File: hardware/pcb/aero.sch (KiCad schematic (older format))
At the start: 2 parts

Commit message: more progress on hw
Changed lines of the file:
@@
 $Descr A4 11693 8268
 encoding utf-8
-Sheet 1 5
+Sheet 1 6
 Title ""
 Date ""
@@
 $EndSheet
 $Sheet
-S 1950 850  700  650
+S 1250 3750 700  650
 U 551EEA41
 F0 "ms5611" 60
 F1 "ms5611.sch" 60
-F2 "EN" I R 2650 1150 60
-F3 "SCLK" I R 2650 1450 60
-F4 "MOSI" I R 2650 1250 60
-F5 "MISO" I R 2650 1350 60
-$EndSheet
-$Sheet
-S 1850 2650 750  900
+F2 "EN" I R 1950 4050 60
+F3 "SCLK" I R 1950 4350 60
+F4 "MOSI" I R 1950 4150 60
+F5 "MISO" I R 1950 4250 60
+$EndSheet
+$Sheet
+S 1300 4800 750  900
 U 5527E8E0
 F0 "bmx055" 60
 F1 "bmx055.sch" 60
-F2 "ACC_SEL" I R 2600 2750 60
-F3 "GYRO_SEL" I R 2600 2850 60
-F4 "MAG_SEL" I R 2600 2950 60
-F5 "ACC_INT" I R 2600 3050 60
-F6 "MISO" I R 2600 3250 60
-F7 "MOSI" I R 2600 3350 60
-F8 "SCK" I R 2600 3450 60
+F2 "ACC_SEL" I R 2050 4900 60
+F3 "GYRO_SEL" I R 2050 5000 60
+F4 "MAG_SEL" I R 2050 5100 60
+F5 "ACC_INT" I R 2050 5200 60
+F6 "MISO" I R 2050 5400 60
+F7 "MOSI" I R 2050 5500 60
+F8 "SCK" I R 2050 5600 60
 $EndSheet
 $Comp
@@
 	9100 2600 9100 3900
 Connection ~ 9100 3900
+$Sheet
+S 1500 1450 800  650
+U 552EDA4D
+F0 "power" 60
+F1 "power.sch" 60
+F2 "+3V" I R 2300 1600 60
+F3 "USB_D-" I R 2300 1750 60
+F4 "USB_D+" I R 2300 1850 60
+$EndSheet
+$Comp
+L +3V #PWR?
+U 1 1 552F0919
+P 2800 1300
+F 0 "#PWR?" H 2800 1200 60  0001 C CNN
+F 1 "+3V" H 2650 1450 60  0000 C CNN
+F 2 "" H 2800 1300 60  0000 C CNN
+F 3 "" H 2800 1300 60  0000 C CNN
+	1    2800 1300
+	1    0    0    -1
+$EndComp
+Wire Wire Line
+	2800 1300 2800 1600
+Wire Wire Line
+	2800 1600 2300 1600
 $EndSCHEMATC

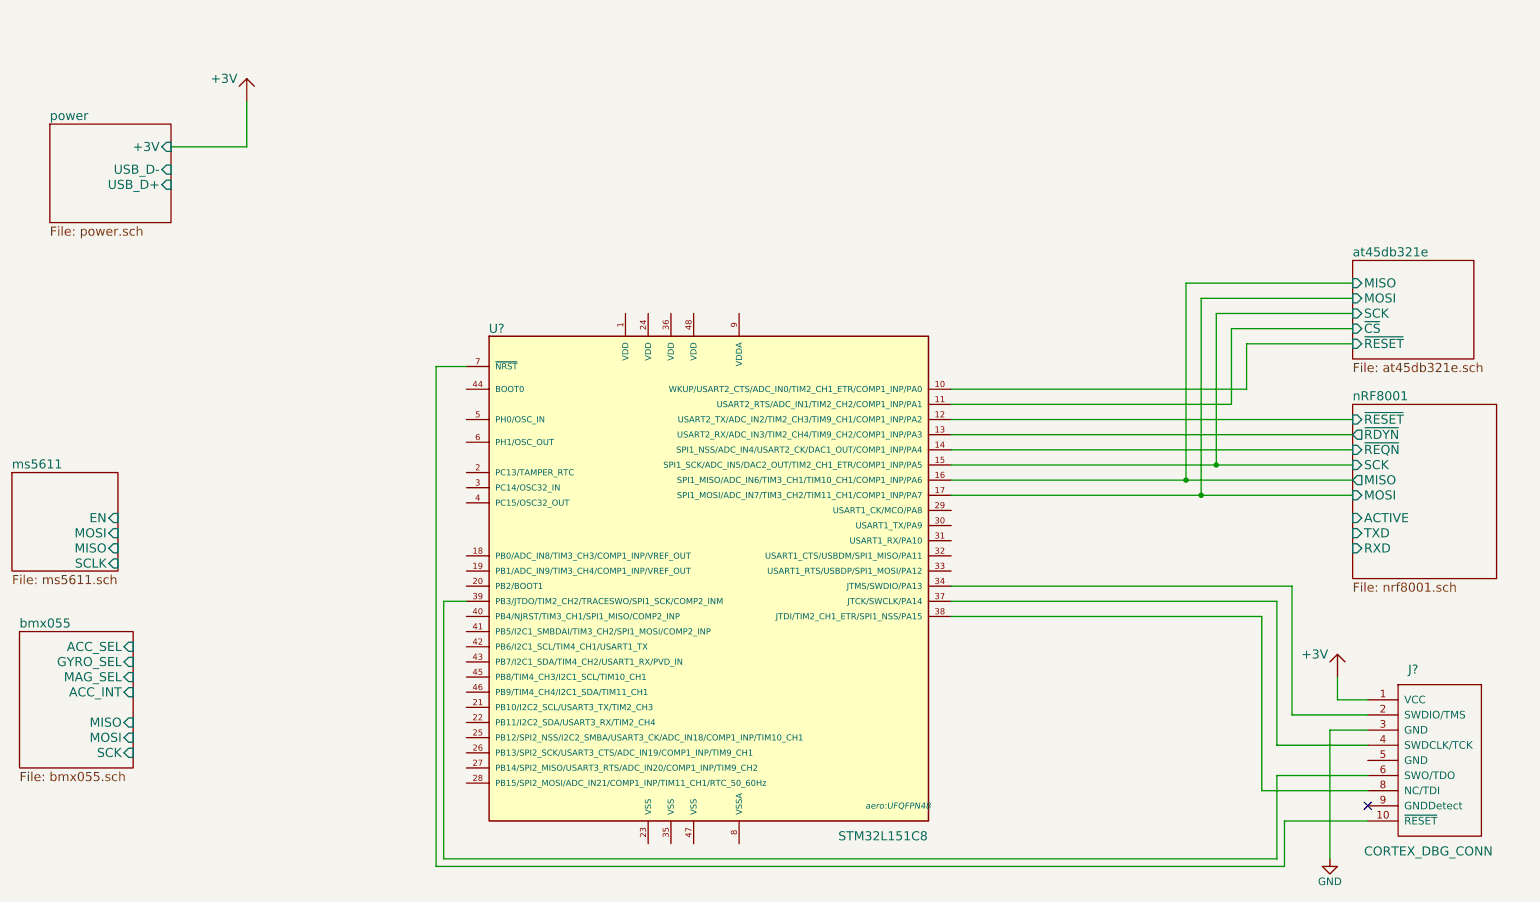
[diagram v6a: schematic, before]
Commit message: More work on power section
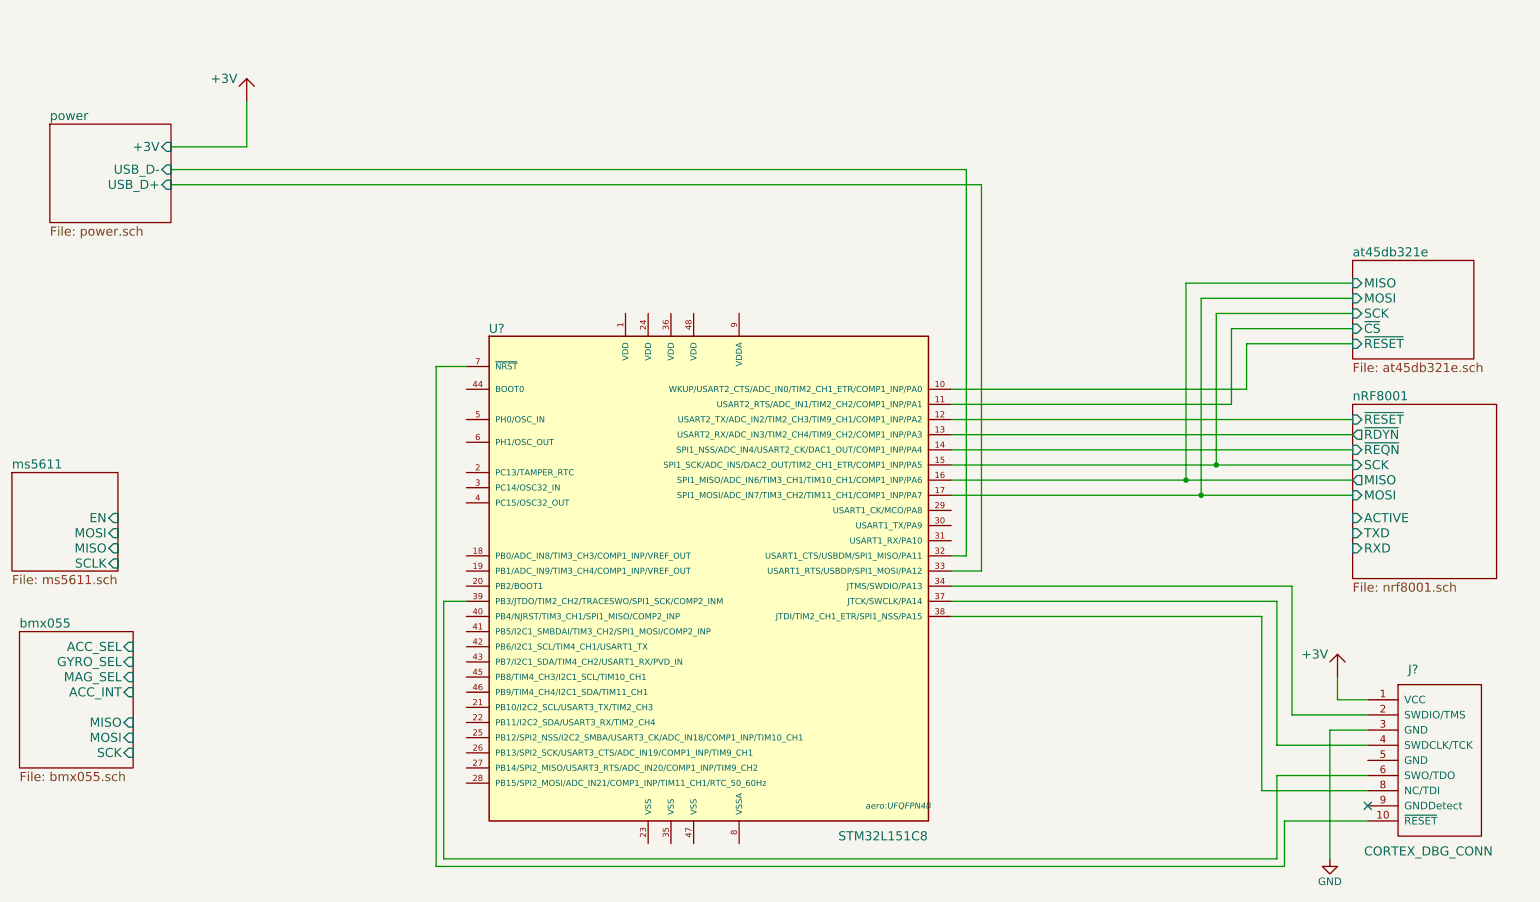
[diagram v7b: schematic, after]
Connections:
- net power/USB_D+: now also U?.33 (USART1_RTS/USBDP/SPI1_MOSI/PA12)
- net power/USB_D-: now also U?.32 (USART1_CTS/USBDM/SPI1_MISO/PA11)
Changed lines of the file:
@@
 Wire Wire Line
 	2800 1600 2300 1600
+Wire Wire Line
+	2300 1750 7550 1750
+Wire Wire Line
+	7550 1750 7550 4300
+Wire Wire Line
+	7550 4300 7450 4300
+Wire Wire Line
+	7450 4400 7650 4400
+Wire Wire Line
+	7650 4400 7650 1850
+Wire Wire Line
+	7650 1850 2300 1850
 $EndSCHEMATC

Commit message: added sensor connections
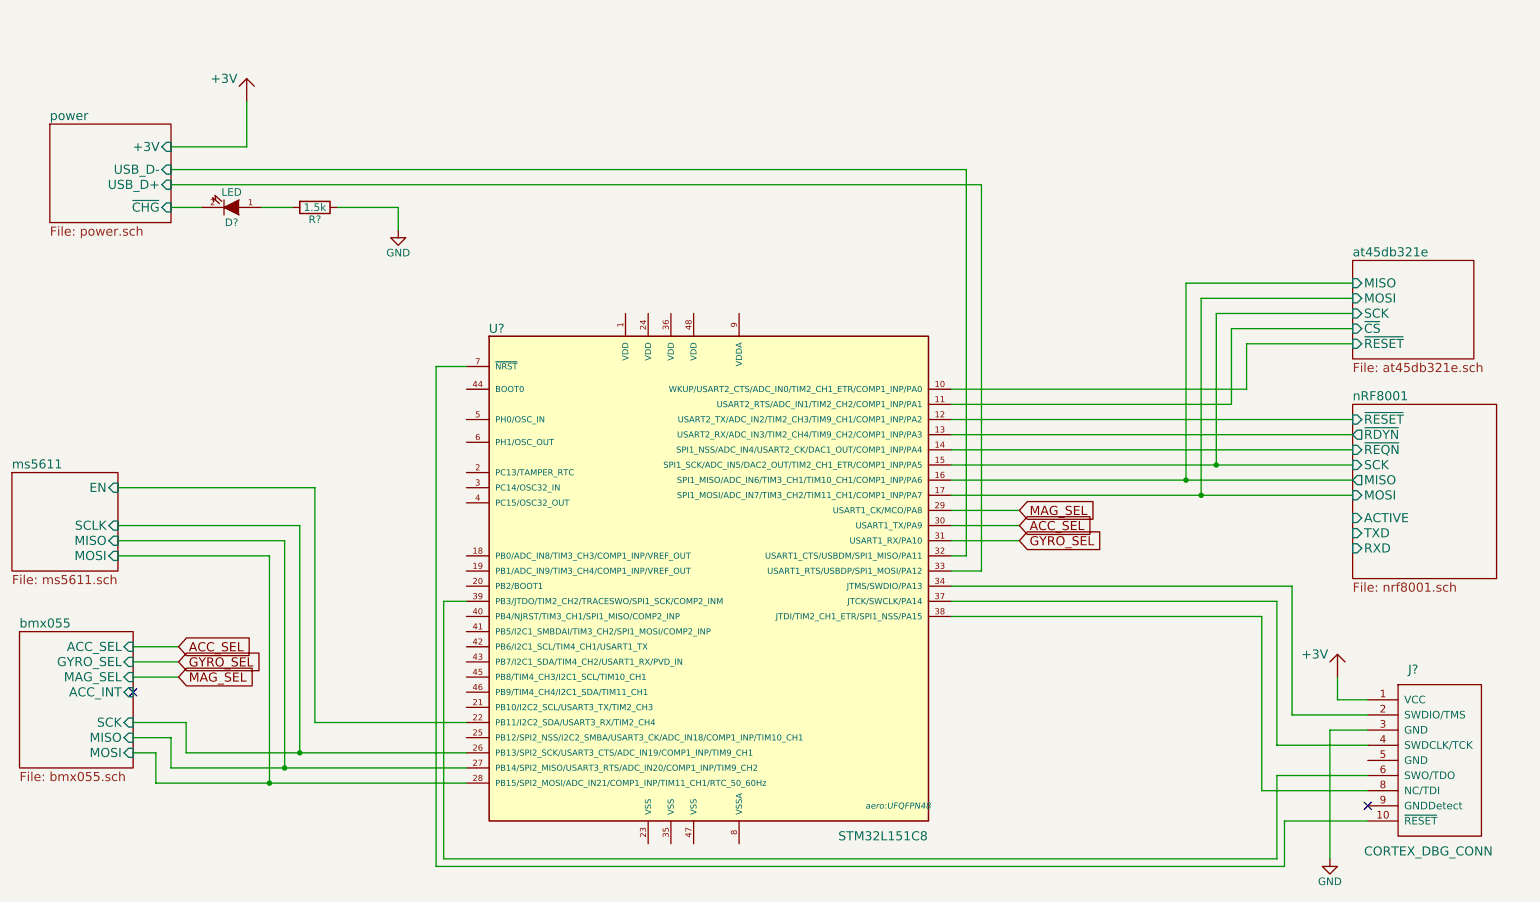
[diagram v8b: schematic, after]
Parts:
- added D?: LED, symbol LED
- added R?: 1.5k, symbol R
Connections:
- net GND: now also R?.1
- net bmx055/MISO: now also U?.27 (PB14/SPI2_MISO/USART3_RTS/ADC_IN20/COMP1_INP/TIM9_CH2)
- net bmx055/MOSI: now also U?.28 (PB15/SPI2_MOSI/ADC_IN21/COMP1_INP/TIM11_CH1/RTC_50_60Hz)
- net bmx055/SCK: now also U?.26 (PB13/SPI2_SCK/USART3_CTS/ADC_IN19/COMP1_INP/TIM9_CH1)
- net ms5611/EN: now also U?.22 (PB11/I2C2_SDA/USART3_RX/TIM2_CH4)
- net MAG_SEL: now reaches U?.29 (USART1_CK/MCO/PA8)
- net ACC_SEL: now reaches U?.30 (USART1_TX/PA9)
- net GYRO_SEL: now reaches U?.31 (USART1_RX/PA10)
- new net: D?.1 (A), R?.2
- new net power/~CHG: D?.2 (K)
- no-connect marks 1 -> 2
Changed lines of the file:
@@
 F0 "ms5611" 60
 F1 "ms5611.sch" 60
-F2 "EN" I R 1950 4050 60
-F3 "SCLK" I R 1950 4350 60
-F4 "MOSI" I R 1950 4150 60
-F5 "MISO" I R 1950 4250 60
+F2 "EN" I R 1950 3850 60
+F3 "SCLK" I R 1950 4100 60
+F4 "MOSI" I R 1950 4300 60
+F5 "MISO" I R 1950 4200 60
 $EndSheet
 $Sheet
@@
 F4 "MAG_SEL" I R 2050 5100 60
 F5 "ACC_INT" I R 2050 5200 60
-F6 "MISO" I R 2050 5400 60
-F7 "MOSI" I R 2050 5500 60
-F8 "SCK" I R 2050 5600 60
+F6 "MISO" I R 2050 5500 60
+F7 "MOSI" I R 2050 5600 60
+F8 "SCK" I R 2050 5400 60
 $EndSheet
 $Comp
@@
 F6 "~RESET" I L 10100 2900 60
 $EndSheet
-Wire Wire Line
-	10100 3900 7450 3900
-Wire Wire Line
-	7450 3700 10100 3700
-Wire Wire Line
-	10100 3800 7450 3800
-Wire Wire Line
-	7450 3600 10100 3600
-Wire Wire Line
-	10100 3500 7450 3500
-Wire Wire Line
-	7450 3400 10100 3400
-Wire Wire Line
-	10200 5250 10000 5250
-Wire Wire Line
-	10000 5250 10000 5100
-Wire Wire Line
-	10200 5350 9700 5350
-Wire Wire Line
-	9700 5350 9700 4500
-Wire Wire Line
-	9700 4500 7450 4500
-Wire Wire Line
-	7450 4600 9600 4600
-Wire Wire Line
-	9600 4600 9600 5550
-Wire Wire Line
-	9600 5550 10200 5550
-Wire Wire Line
-	4250 4600 4100 4600
-Wire Wire Line
-	4100 4600 4100 6300
-Wire Wire Line
-	4100 6300 9600 6300
-Wire Wire Line
-	9600 6300 9600 5750
-Wire Wire Line
-	9600 5750 10200 5750
-Wire Wire Line
-	7450 4700 9500 4700
-Wire Wire Line
-	9500 4700 9500 5850
-Wire Wire Line
-	9500 5850 10200 5850
-Wire Wire Line
-	10200 5450 9950 5450
-Wire Wire Line
-	9950 5450 9950 6300
-Wire Wire Line
-	10100 2500 9000 2500
-Wire Wire Line
-	9000 2500 9000 3800
-Connection ~ 9000 3800
-Wire Wire Line
-	10100 2700 9200 2700
-Wire Wire Line
-	9200 2700 9200 3700
-Connection ~ 9200 3700
-Wire Wire Line
-	10100 2800 9300 2800
-Wire Wire Line
-	9300 2800 9300 3300
-Wire Wire Line
-	9300 3300 7450 3300
-Wire Wire Line
-	10100 2900 9400 2900
-Wire Wire Line
-	9400 2900 9400 3200
-Wire Wire Line
-	9400 3200 7450 3200
-Wire Wire Line
-	10200 6050 9650 6050
-Wire Wire Line
-	9650 6050 9650 6350
-Wire Wire Line
-	9650 6350 4050 6350
-Wire Wire Line
-	4050 6350 4050 3050
-Wire Wire Line
-	4050 3050 4250 3050
-Wire Wire Line
-	10100 2600 9100 2600
-Wire Wire Line
-	9100 2600 9100 3900
-Connection ~ 9100 3900
 $Sheet
 S 1500 1450 800  650
@@
 F3 "USB_D-" I R 2300 1750 60
 F4 "USB_D+" I R 2300 1850 60
+F5 "~CHG" I R 2300 2000 60
 $EndSheet
 $Comp
@@
 	1    0    0    -1
 $EndComp
+$Comp
+L LED D?
+U 1 1 553048D5
+P 2700 2000
+F 0 "D?" H 2700 2100 50  0000 C CNN
+F 1 "LED" H 2700 1900 50  0000 C CNN
+F 2 "" H 2700 2000 60  0000 C CNN
+F 3 "" H 2700 2000 60  0000 C CNN
+	1    2700 2000
+	-1   0    0    1
+$EndComp
+$Comp
+L R R?
+U 1 1 553049A8
+P 3250 2000
+F 0 "R?" V 3330 2000 50  0000 C CNN
+F 1 "1.5k" V 3250 2000 50  0000 C CNN
+F 2 "" V 3180 2000 30  0000 C CNN
+F 3 "" H 3250 2000 30  0000 C CNN
+	1    3250 2000
+	0    1    1    0
+$EndComp
+$Comp
+L GND #PWR?
+U 1 1 55304B43
+P 3800 2150
+F 0 "#PWR?" H 3800 1900 50  0001 C CNN
+F 1 "GND" H 3800 2000 50  0000 C CNN
+F 2 "" H 3800 2150 60  0000 C CNN
+F 3 "" H 3800 2150 60  0000 C CNN
+	1    3800 2150
+	1    0    0    -1
+$EndComp
+Text GLabel 7900 4100 2    60   Input ~ 0
+ACC_SEL
+Text GLabel 7900 4200 2    60   Input ~ 0
+GYRO_SEL
+Text GLabel 7900 4000 2    60   Input ~ 0
+MAG_SEL
+Text GLabel 2350 5100 2    60   Input ~ 0
+MAG_SEL
+Text GLabel 2350 5000 2    60   Input ~ 0
+GYRO_SEL
+Text GLabel 2350 4900 2    60   Input ~ 0
+ACC_SEL
+Wire Wire Line
+	10100 3900 7450 3900
+Wire Wire Line
+	7450 3700 10100 3700
+Wire Wire Line
+	10100 3800 7450 3800
+Wire Wire Line
+	7450 3600 10100 3600
+Wire Wire Line
+	10100 3500 7450 3500
+Wire Wire Line
+	7450 3400 10100 3400
+Wire Wire Line
+	10200 5250 10000 5250
+Wire Wire Line
+	10000 5250 10000 5100
+Wire Wire Line
+	10200 5350 9700 5350
+Wire Wire Line
+	9700 5350 9700 4500
+Wire Wire Line
+	9700 4500 7450 4500
+Wire Wire Line
+	7450 4600 9600 4600
+Wire Wire Line
+	9600 4600 9600 5550
+Wire Wire Line
+	9600 5550 10200 5550
+Wire Wire Line
+	4250 4600 4100 4600
+Wire Wire Line
+	4100 4600 4100 6300
+Wire Wire Line
+	4100 6300 9600 6300
+Wire Wire Line
+	9600 6300 9600 5750
+Wire Wire Line
+	9600 5750 10200 5750
+Wire Wire Line
+	7450 4700 9500 4700
+Wire Wire Line
+	9500 4700 9500 5850
+Wire Wire Line
+	9500 5850 10200 5850
+Wire Wire Line
+	10200 5450 9950 5450
+Wire Wire Line
+	9950 5450 9950 6300
+Wire Wire Line
+	10100 2500 9000 2500
+Wire Wire Line
+	9000 2500 9000 3800
+Connection ~ 9000 3800
+Wire Wire Line
+	10100 2700 9200 2700
+Wire Wire Line
+	9200 2700 9200 3700
+Connection ~ 9200 3700
+Wire Wire Line
+	10100 2800 9300 2800
+Wire Wire Line
+	9300 2800 9300 3300
+Wire Wire Line
+	9300 3300 7450 3300
+Wire Wire Line
+	10100 2900 9400 2900
+Wire Wire Line
+	9400 2900 9400 3200
+Wire Wire Line
+	9400 3200 7450 3200
+Wire Wire Line
+	10200 6050 9650 6050
+Wire Wire Line
+	9650 6050 9650 6350
+Wire Wire Line
+	9650 6350 4050 6350
+Wire Wire Line
+	4050 6350 4050 3050
+Wire Wire Line
+	4050 3050 4250 3050
+Wire Wire Line
+	10100 2600 9100 2600
+Wire Wire Line
+	9100 2600 9100 3900
+Connection ~ 9100 3900
 Wire Wire Line
 	2800 1300 2800 1600
@@
 Wire Wire Line
 	7650 1850 2300 1850
+Wire Wire Line
+	3400 2000 3800 2000
+Wire Wire Line
+	3800 2000 3800 2150
+Wire Wire Line
+	3100 2000 2900 2000
+Wire Wire Line
+	2500 2000 2300 2000
+Wire Wire Line
+	7900 4000 7450 4000
+Wire Wire Line
+	7900 4100 7450 4100
+Wire Wire Line
+	7900 4200 7450 4200
+Wire Wire Line
+	2050 4900 2350 4900
+Wire Wire Line
+	2350 5000 2050 5000
+Wire Wire Line
+	2050 5100 2350 5100
+NoConn ~ 2050 5200
+Wire Wire Line
+	4250 5800 2200 5800
+Wire Wire Line
+	2200 5800 2200 5600
+Wire Wire Line
+	2200 5600 2050 5600
+Wire Wire Line
+	2050 5500 2300 5500
+Wire Wire Line
+	2300 5500 2300 5700
+Wire Wire Line
+	2300 5700 4250 5700
+Wire Wire Line
+	2050 5400 2400 5400
+Wire Wire Line
+	2400 5400 2400 5600
+Wire Wire Line
+	2400 5600 4250 5600
+Wire Wire Line
+	1950 4300 2950 4300
+Wire Wire Line
+	2950 4300 2950 5800
+Connection ~ 2950 5800
+Wire Wire Line
+	1950 4200 3050 4200
+Wire Wire Line
+	3050 4200 3050 5700
+Connection ~ 3050 5700
+Wire Wire Line
+	1950 4100 3150 4100
+Wire Wire Line
+	3150 4100 3150 5600
+Connection ~ 3150 5600
+Wire Wire Line
+	1950 3850 3250 3850
+Wire Wire Line
+	3250 3850 3250 5400
+Wire Wire Line
+	3250 5400 4250 5400
 $EndSCHEMATC
